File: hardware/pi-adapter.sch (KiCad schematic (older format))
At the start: 32 parts, among them P1 CONN_02X20, P10 CONN_01X04, P11 CONN_01X04, P12 CONN_01X04, P13 CONN_01X04, P14 CONN_01X04, P15 CONN_01X04, P16 CONN_01X04, P17 CONN_01X04, P18 CONN_01X04, P19 CONN_01X04, P2 +5V, P20 CONN_01X04, P21 CONN_01X04, P22 CONN_01X06, P3 CONN_01X03, P4 GND, P5 CONN_01X03, P6 CONN_01X04, P7 CONN_01X04, P8 CONN_01X04, P9 CONN_01X04, U1 74HCT245, U2 74HCT245, U3 74HCT245, U4 74HCT245

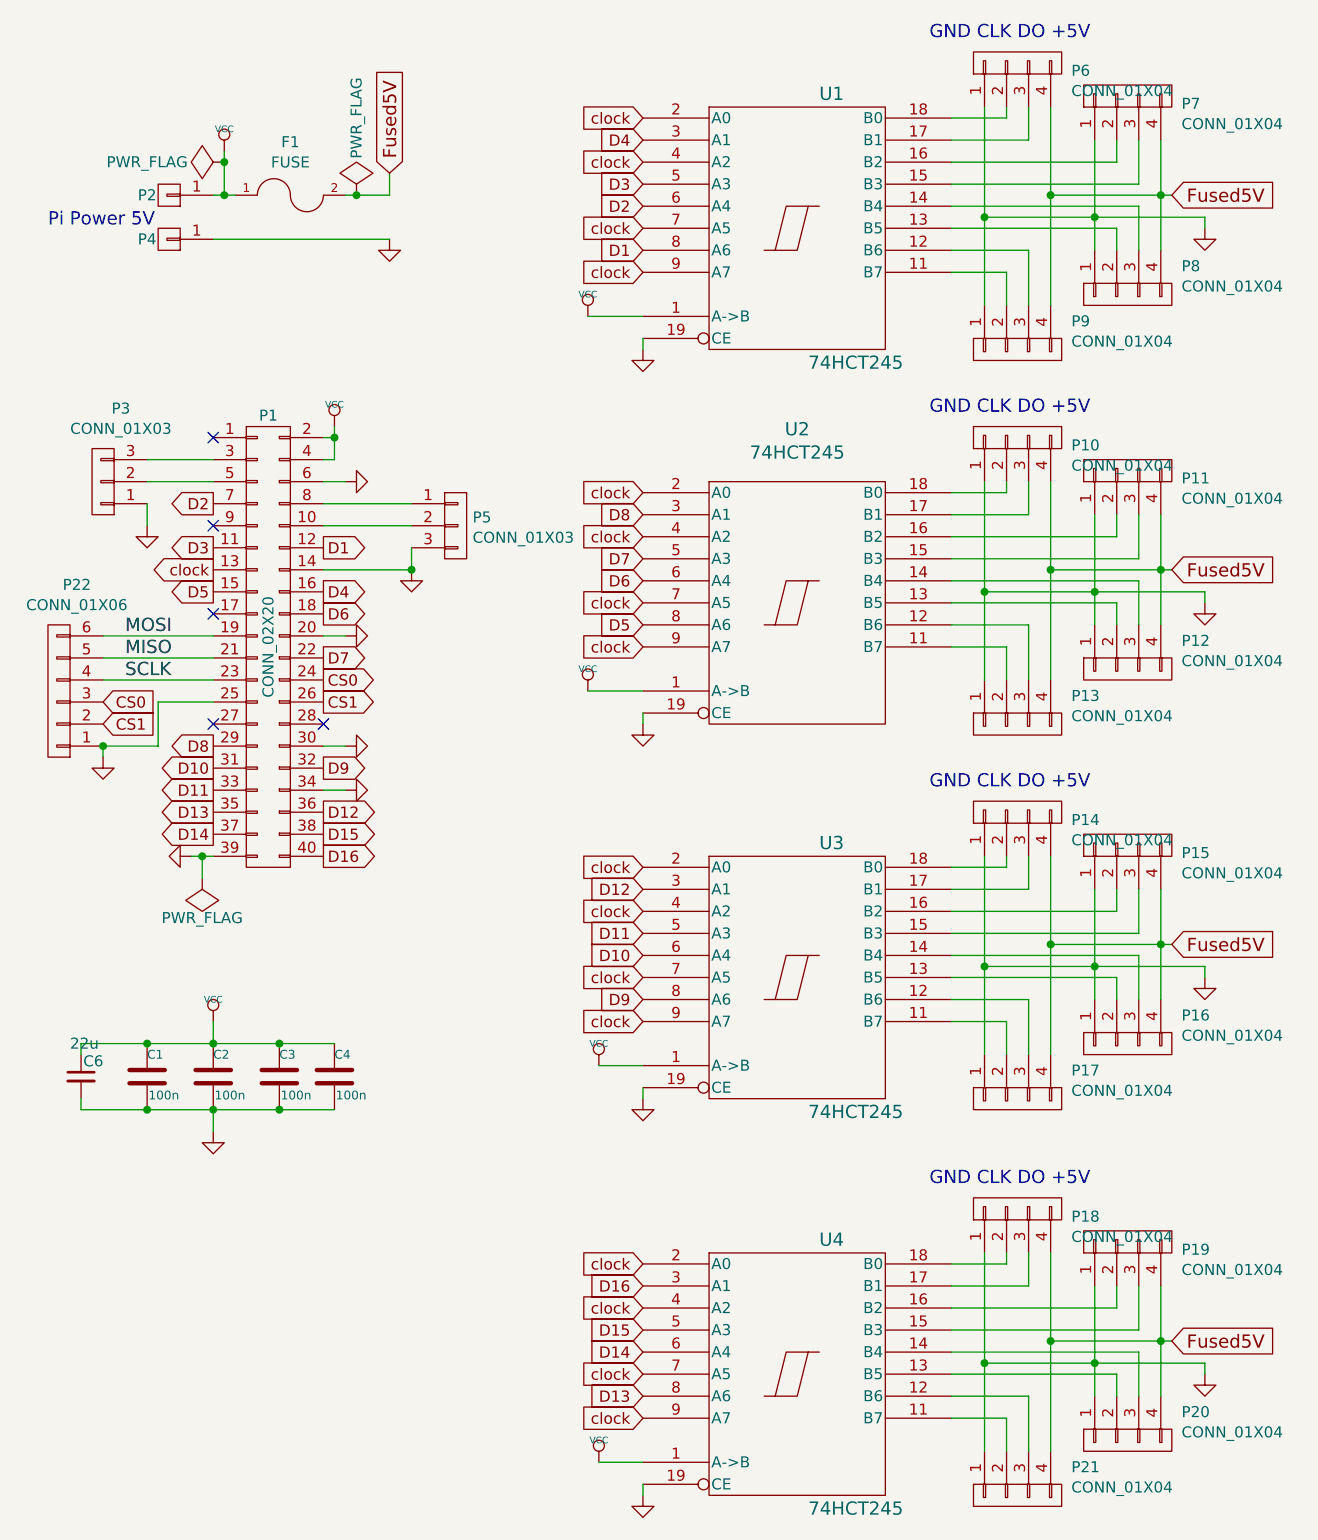
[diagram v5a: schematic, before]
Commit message: o Rename header references for easier connecting.
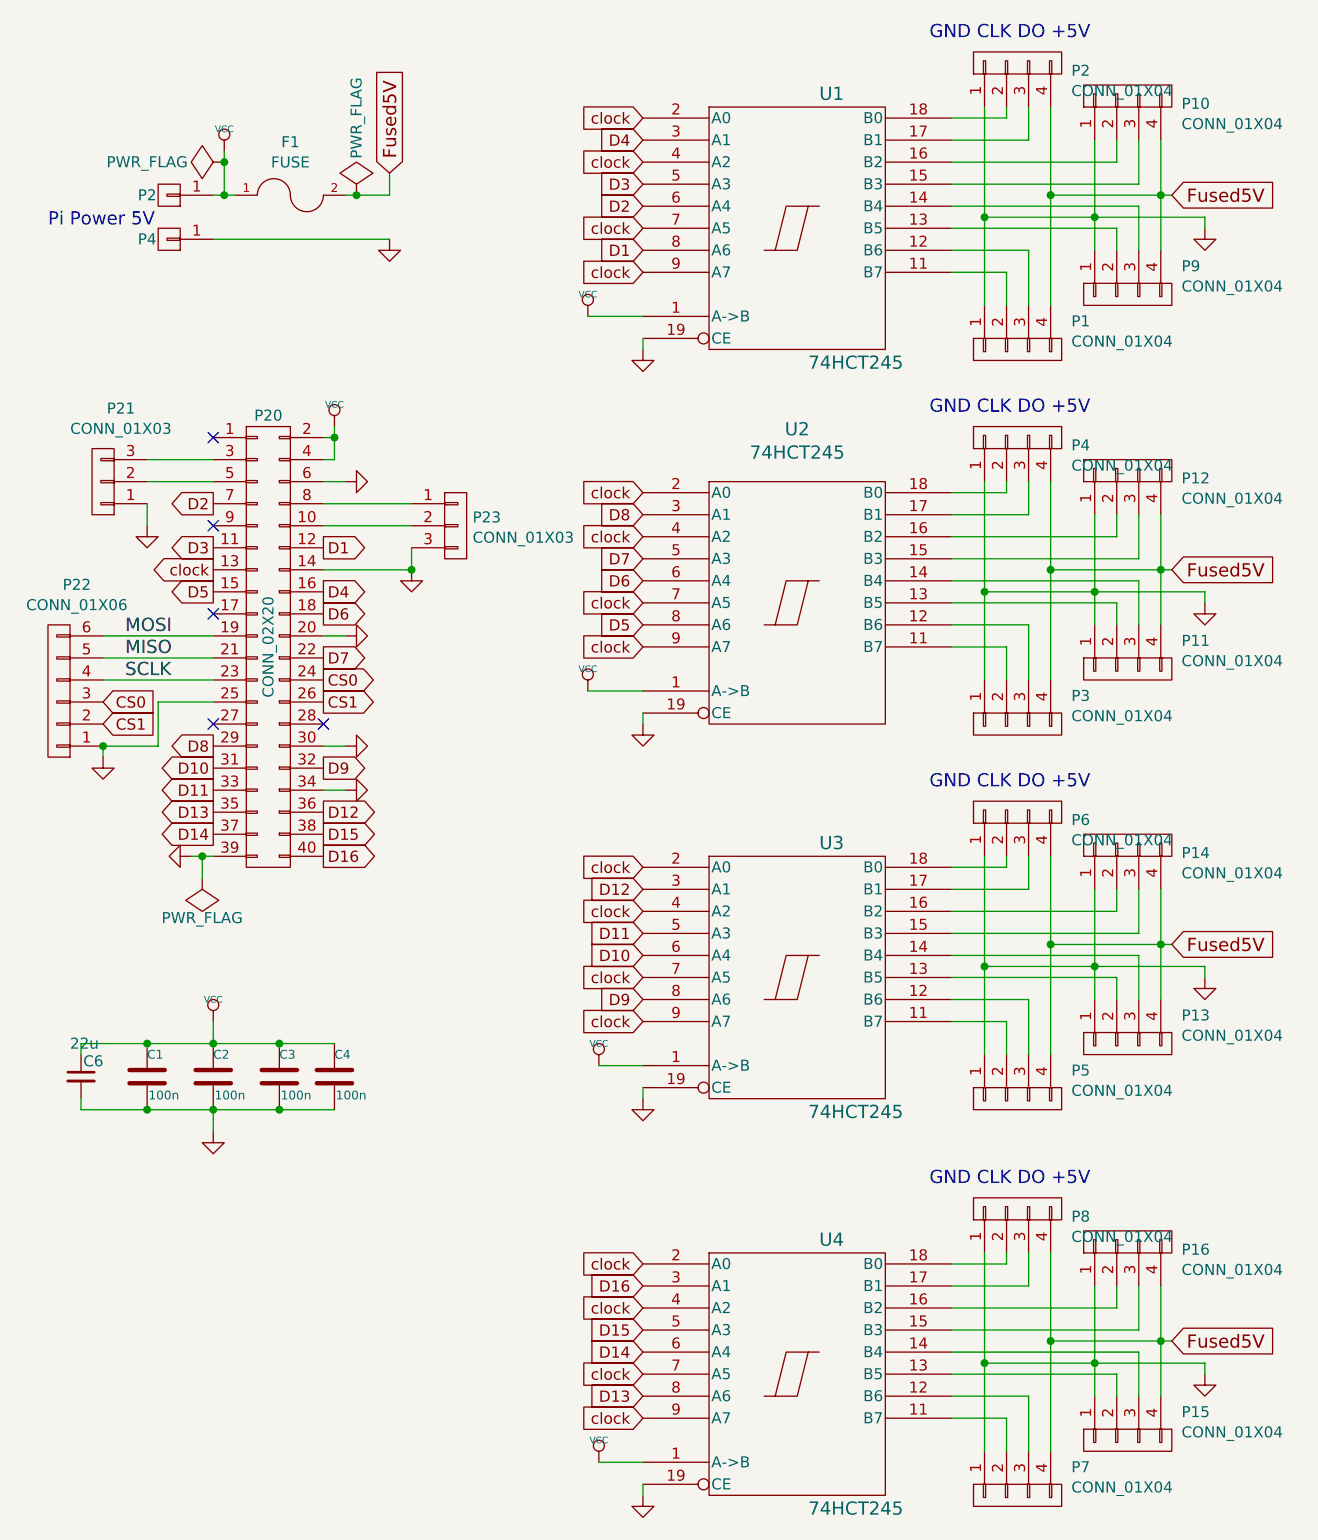
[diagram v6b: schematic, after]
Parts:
- renumbered P9 to P1, P7 to P10, P12 to P11, P11 to P12, P16 to P13, P15 to P14, P20 to P15, P19 to P16, P6 to P2, P1 to P20, P3 to P21, P5 to P23, P13 to P3, P10 to P4, P17 to P5, P14 to P6, P21 to P7, P18 to P8, P8 to P9
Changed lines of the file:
@@
 clock
 $Comp
-L CONN_01X04 P6
+L CONN_01X04 P2
 U 1 1 56C16676
 P 5550 1000
-F 0 "P6" V 5515 756 50  0000 R CNN
+F 0 "P2" V 5515 756 50  0000 R CNN
 F 1 "CONN_01X04" V 5423 756 50  0000 R CNN
 F 2 "Pin_Headers:Pin_Header_Straight_1x04" V 5377 756 50  0001 R CNN
@@
 $EndComp
 $Comp
-L CONN_01X04 P9
+L CONN_01X04 P1
 U 1 1 56C1694E
 P 5550 2300
-F 0 "P9" V 5422 2056 50  0000 R CNN
+F 0 "P1" V 5422 2056 50  0000 R CNN
 F 1 "CONN_01X04" V 5514 2056 50  0000 R CNN
 F 2 "Pin_Headers:Pin_Header_Straight_1x04" V 5377 2056 50  0001 R CNN
@@
 $EndComp
 $Comp
-L CONN_01X04 P7
+L CONN_01X04 P10
 U 1 1 56C16C70
 P 6050 1150
-F 0 "P7" V 6015 906 50  0000 R CNN
+F 0 "P10" V 6015 906 50  0000 R CNN
 F 1 "CONN_01X04" V 5923 906 50  0000 R CNN
 F 2 "Pin_Headers:Pin_Header_Straight_1x04" H 6050 1150 50  0001 C CNN
@@
 	5250 1850 5600 1850
 $Comp
-L CONN_01X04 P8
+L CONN_01X04 P9
 U 1 1 56C17042
 P 6050 2050
-F 0 "P8" V 5922 1806 50  0000 R CNN
+F 0 "P9" V 5922 1806 50  0000 R CNN
 F 1 "CONN_01X04" V 6014 1806 50  0000 R CNN
 F 2 "Pin_Headers:Pin_Header_Straight_1x04" V 5877 1806 50  0001 R CNN
@@
 $EndComp
 $Comp
-L CONN_02X20 P1
+L CONN_02X20 P20
 U 1 1 54ECB2B7
 P 2150 3650
-F 0 "P1" H 2150 4700 50  0000 C CNN
+F 0 "P20" H 2150 4700 50  0000 C CNN
 F 1 "CONN_02X20" V 2150 3650 50  0000 C CNN
 F 2 "Pin_Headers:Pin_Header_Straight_2x20" H 2150 2700 60  0001 C CNN
@@
 $EndComp
 $Comp
-L CONN_01X03 P5
+L CONN_01X03 P23
 U 1 1 56C196A7
 P 3000 3100
-F 0 "P5" H 3077 3138 50  0000 L CNN
+F 0 "P23" H 3077 3138 50  0000 L CNN
 F 1 "CONN_01X03" H 3077 3046 50  0000 L CNN
 F 2 "Pin_Headers:Pin_Header_Straight_1x03" H 3000 3100 50  0001 C CNN
@@
 $EndComp
 $Comp
-L CONN_01X03 P3
+L CONN_01X03 P21
 U 1 1 56C19AA9
 P 1400 2900
-F 0 "P3" H 1319 2568 50  0000 C CNN
+F 0 "P21" H 1319 2568 50  0000 C CNN
 F 1 "CONN_01X03" H 1319 2660 50  0000 C CNN
 F 2 "Pin_Headers:Pin_Header_Straight_1x03" H 1400 2900 50  0001 C CNN
@@
 GND CLK DO +5V\n
 $Comp
-L CONN_01X04 P10
+L CONN_01X04 P4
 U 1 1 56C22C41
 P 5550 2700
-F 0 "P10" V 5515 2456 50  0000 R CNN
+F 0 "P4" V 5515 2456 50  0000 R CNN
 F 1 "CONN_01X04" V 5423 2456 50  0000 R CNN
 F 2 "Pin_Headers:Pin_Header_Straight_1x04" V 5377 2456 50  0001 R CNN
@@
 $EndComp
 $Comp
-L CONN_01X04 P13
+L CONN_01X04 P3
 U 1 1 56C22C47
 P 5550 4000
-F 0 "P13" V 5422 3756 50  0000 R CNN
+F 0 "P3" V 5422 3756 50  0000 R CNN
 F 1 "CONN_01X04" V 5514 3756 50  0000 R CNN
 F 2 "Pin_Headers:Pin_Header_Straight_1x04" V 5377 3756 50  0001 R CNN
@@
 $EndComp
 $Comp
-L CONN_01X04 P11
+L CONN_01X04 P12
 U 1 1 56C22C4D
 P 6050 2850
-F 0 "P11" V 6015 2606 50  0000 R CNN
+F 0 "P12" V 6015 2606 50  0000 R CNN
 F 1 "CONN_01X04" V 5923 2606 50  0000 R CNN
 F 2 "Pin_Headers:Pin_Header_Straight_1x04" H 6050 2850 50  0001 C CNN
@@
 	5250 3550 5600 3550
 $Comp
-L CONN_01X04 P12
+L CONN_01X04 P11
 U 1 1 56C22C58
 P 6050 3750
-F 0 "P12" V 5922 3506 50  0000 R CNN
+F 0 "P11" V 5922 3506 50  0000 R CNN
 F 1 "CONN_01X04" V 6014 3506 50  0000 R CNN
 F 2 "Pin_Headers:Pin_Header_Straight_1x04" V 5877 3506 50  0001 R CNN
@@
 GND CLK DO +5V\n
 $Comp
-L CONN_01X04 P14
+L CONN_01X04 P6
 U 1 1 56C22D24
 P 5550 4400
-F 0 "P14" V 5515 4156 50  0000 R CNN
+F 0 "P6" V 5515 4156 50  0000 R CNN
 F 1 "CONN_01X04" V 5423 4156 50  0000 R CNN
 F 2 "Pin_Headers:Pin_Header_Straight_1x04" V 5377 4156 50  0001 R CNN
@@
 $EndComp
 $Comp
-L CONN_01X04 P17
+L CONN_01X04 P5
 U 1 1 56C22D2A
 P 5550 5700
-F 0 "P17" V 5422 5456 50  0000 R CNN
+F 0 "P5" V 5422 5456 50  0000 R CNN
 F 1 "CONN_01X04" V 5514 5456 50  0000 R CNN
 F 2 "Pin_Headers:Pin_Header_Straight_1x04" V 5377 5456 50  0001 R CNN
@@
 $EndComp
 $Comp
-L CONN_01X04 P15
+L CONN_01X04 P14
 U 1 1 56C22D30
 P 6050 4550
-F 0 "P15" V 6015 4306 50  0000 R CNN
+F 0 "P14" V 6015 4306 50  0000 R CNN
 F 1 "CONN_01X04" V 5923 4306 50  0000 R CNN
 F 2 "Pin_Headers:Pin_Header_Straight_1x04" H 6050 4550 50  0001 C CNN
@@
 	5250 5250 5600 5250
 $Comp
-L CONN_01X04 P16
+L CONN_01X04 P13
 U 1 1 56C22D3B
 P 6050 5450
-F 0 "P16" V 5922 5206 50  0000 R CNN
+F 0 "P13" V 5922 5206 50  0000 R CNN
 F 1 "CONN_01X04" V 6014 5206 50  0000 R CNN
 F 2 "Pin_Headers:Pin_Header_Straight_1x04" V 5877 5206 50  0001 R CNN
@@
 GND CLK DO +5V\n
 $Comp
-L CONN_01X04 P18
+L CONN_01X04 P8
 U 1 1 56C22EEF
 P 5550 6200
-F 0 "P18" V 5515 5956 50  0000 R CNN
+F 0 "P8" V 5515 5956 50  0000 R CNN
 F 1 "CONN_01X04" V 5423 5956 50  0000 R CNN
 F 2 "Pin_Headers:Pin_Header_Straight_1x04" V 5377 5956 50  0001 R CNN
@@
 $EndComp
 $Comp
-L CONN_01X04 P21
+L CONN_01X04 P7
 U 1 1 56C22EF5
 P 5550 7500
-F 0 "P21" V 5422 7256 50  0000 R CNN
+F 0 "P7" V 5422 7256 50  0000 R CNN
 F 1 "CONN_01X04" V 5514 7256 50  0000 R CNN
 F 2 "Pin_Headers:Pin_Header_Straight_1x04" V 5377 7256 50  0001 R CNN
@@
 $EndComp
 $Comp
-L CONN_01X04 P19
+L CONN_01X04 P16
 U 1 1 56C22EFB
 P 6050 6350
-F 0 "P19" V 6015 6106 50  0000 R CNN
+F 0 "P16" V 6015 6106 50  0000 R CNN
 F 1 "CONN_01X04" V 5923 6106 50  0000 R CNN
 F 2 "Pin_Headers:Pin_Header_Straight_1x04" H 6050 6350 50  0001 C CNN
@@
 	5250 7050 5600 7050
 $Comp
-L CONN_01X04 P20
+L CONN_01X04 P15
 U 1 1 56C22F06
 P 6050 7250
-F 0 "P20" V 5922 7006 50  0000 R CNN
+F 0 "P15" V 5922 7006 50  0000 R CNN
 F 1 "CONN_01X04" V 6014 7006 50  0000 R CNN
 F 2 "Pin_Headers:Pin_Header_Straight_1x04" V 5877 7006 50  0001 R CNN

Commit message: o Some more renaming needed.
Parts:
- renumbered P2 to P30, P4 to P31
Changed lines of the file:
@@
 NoConn ~ 1900 3500
 $Comp
-L PWR_FLAG #FLG017
+L PWR_FLAG #FLG016
 U 1 1 557B23A7
 P 1850 4700
-F 0 "#FLG017" H 1850 4795 50  0001 C CNN
+F 0 "#FLG016" H 1850 4795 50  0001 C CNN
 F 1 "PWR_FLAG" H 1850 4880 50  0000 C CNN
 F 2 "" H 1850 4700 60  0000 C CNN
@@
 Connection ~ 1850 4600
 $Comp
-L GND #PWR018
+L GND #PWR017
 U 1 1 562B120F
 P 2700 1800
-F 0 "#PWR018" H 2700 1800 30  0001 C CNN
+F 0 "#PWR017" H 2700 1800 30  0001 C CNN
 F 1 "GND" H 2700 1730 30  0001 C CNN
 F 2 "" H 2700 1800 60  0000 C CNN
@@
 $EndComp
 $Comp
-L VCC #PWR019
+L VCC #PWR018
 U 1 1 562B12CC
 P 1950 1400
-F 0 "#PWR019" H 1950 1500 30  0001 C CNN
+F 0 "#PWR018" H 1950 1500 30  0001 C CNN
 F 1 "VCC" H 1950 1500 30  0000 C CNN
 F 2 "" H 1950 1400 60  0000 C CNN
@@
 $EndComp
 $Comp
-L CONN_01X01 P2
+L CONN_01X01 P30
 U 1 1 562B3873
 P 1700 1600
-F 0 "P2" H 1800 1600 50  0000 C CNN
+F 0 "P30" H 1800 1600 50  0000 C CNN
 F 1 "+5V" V 1800 1600 50  0001 C CNN
 F 2 "Pin_Headers:Pin_Header_Straight_1x01" H 1700 1600 60  0001 C CNN
@@
 $EndComp
 $Comp
-L CONN_01X01 P4
+L CONN_01X01 P31
 U 1 1 562B38C3
 P 1700 1800
-F 0 "P4" H 1800 1800 50  0000 C CNN
+F 0 "P31" H 1800 1800 50  0000 C CNN
 F 1 "GND" V 1800 1800 50  0001 C CNN
 F 2 "Pin_Headers:Pin_Header_Straight_1x01" H 1700 1800 60  0001 C CNN
@@
 	5900 1350 5900 1850
 $Comp
-L GND #PWR020
+L GND #PWR019
 U 1 1 56C176D3
 P 6400 1750
-F 0 "#PWR020" H 6400 1750 30  0001 C CNN
+F 0 "#PWR019" H 6400 1750 30  0001 C CNN
 F 1 "GND" H 6400 1680 30  0001 C CNN
 F 2 "" H 6400 1750 60  0000 C CNN
@@
 $EndComp
 $Comp
-L GND #PWR021
+L GND #PWR020
 U 1 1 56C198BA
 P 2800 3300
-F 0 "#PWR021" H 2800 3300 30  0001 C CNN
+F 0 "#PWR020" H 2800 3300 30  0001 C CNN
 F 1 "GND" H 2800 3230 30  0001 C CNN
 F 2 "" H 2800 3300 60  0000 C CNN
@@
 	1600 2900 1900 2900
 $Comp
-L GND #PWR022
+L GND #PWR021
 U 1 1 56C19EE1
 P 1600 3100
-F 0 "#PWR022" H 1600 3100 30  0001 C CNN
+F 0 "#PWR021" H 1600 3100 30  0001 C CNN
 F 1 "GND" H 1600 3030 30  0001 C CNN
 F 2 "" H 1600 3100 60  0000 C CNN
@@
 Connection ~ 1950 1600
 $Comp
-L VCC #PWR023
+L VCC #PWR022
 U 1 1 56C22E4F
 P 2450 2650
-F 0 "#PWR023" H 2450 2750 30  0001 C CNN
+F 0 "#PWR022" H 2450 2750 30  0001 C CNN
 F 1 "VCC" H 2450 2750 30  0000 C CNN
 F 2 "" H 2450 2650 60  0000 C CNN
@@
 	5900 3050 5900 3550
 $Comp
-L GND #PWR024
+L GND #PWR023
 U 1 1 56C22C65
 P 6400 3450
-F 0 "#PWR024" H 6400 3450 30  0001 C CNN
+F 0 "#PWR023" H 6400 3450 30  0001 C CNN
 F 1 "GND" H 6400 3380 30  0001 C CNN
 F 2 "" H 6400 3450 60  0000 C CNN
@@
 	5900 4750 5900 5250
 $Comp
-L GND #PWR025
+L GND #PWR024
 U 1 1 56C22D48
 P 6400 5150
-F 0 "#PWR025" H 6400 5150 30  0001 C CNN
+F 0 "#PWR024" H 6400 5150 30  0001 C CNN
 F 1 "GND" H 6400 5080 30  0001 C CNN
 F 2 "" H 6400 5150 60  0000 C CNN
@@
 	5900 6550 5900 7050
 $Comp
-L GND #PWR026
+L GND #PWR025
 U 1 1 56C22F13
 P 6400 6950
-F 0 "#PWR026" H 6400 6950 30  0001 C CNN
+F 0 "#PWR025" H 6400 6950 30  0001 C CNN
 F 1 "GND" H 6400 6880 30  0001 C CNN
 F 2 "" H 6400 6950 60  0000 C CNN
@@
 SCLK
 $Comp
-L PWR_FLAG #FLG?
+L PWR_FLAG #FLG026
 U 1 1 56CA81D8
 P 2550 1600
-F 0 "#FLG?" H 2550 1695 50  0001 C CNN
+F 0 "#FLG026" H 2550 1695 50  0001 C CNN
 F 1 "PWR_FLAG" V 2550 1950 50  0000 C CNN
 F 2 "" H 2550 1600 60  0000 C CNN
@@
 	1950 1400 1950 1600
 $Comp
-L PWR_FLAG #FLG?
+L PWR_FLAG #FLG027
 U 1 1 56CA8545
 P 1950 1450
-F 0 "#FLG?" H 1950 1545 50  0001 C CNN
+F 0 "#FLG027" H 1950 1545 50  0001 C CNN
 F 1 "PWR_FLAG" V 1950 1800 50  0000 C CNN
 F 2 "" H 1950 1450 60  0000 C CNN
@@
 	2400 2700 2450 2700
 $Comp
-L GND #PWR?
+L GND #PWR028
 U 1 1 56CF0349
 P 2500 4100
-F 0 "#PWR?" H 2500 4100 30  0001 C CNN
+F 0 "#PWR028" H 2500 4100 30  0001 C CNN
 F 1 "GND" H 2500 4030 30  0001 C CNN
 F 2 "" H 2500 4100 60  0000 C CNN
